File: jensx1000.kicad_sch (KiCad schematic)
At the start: 0 parts

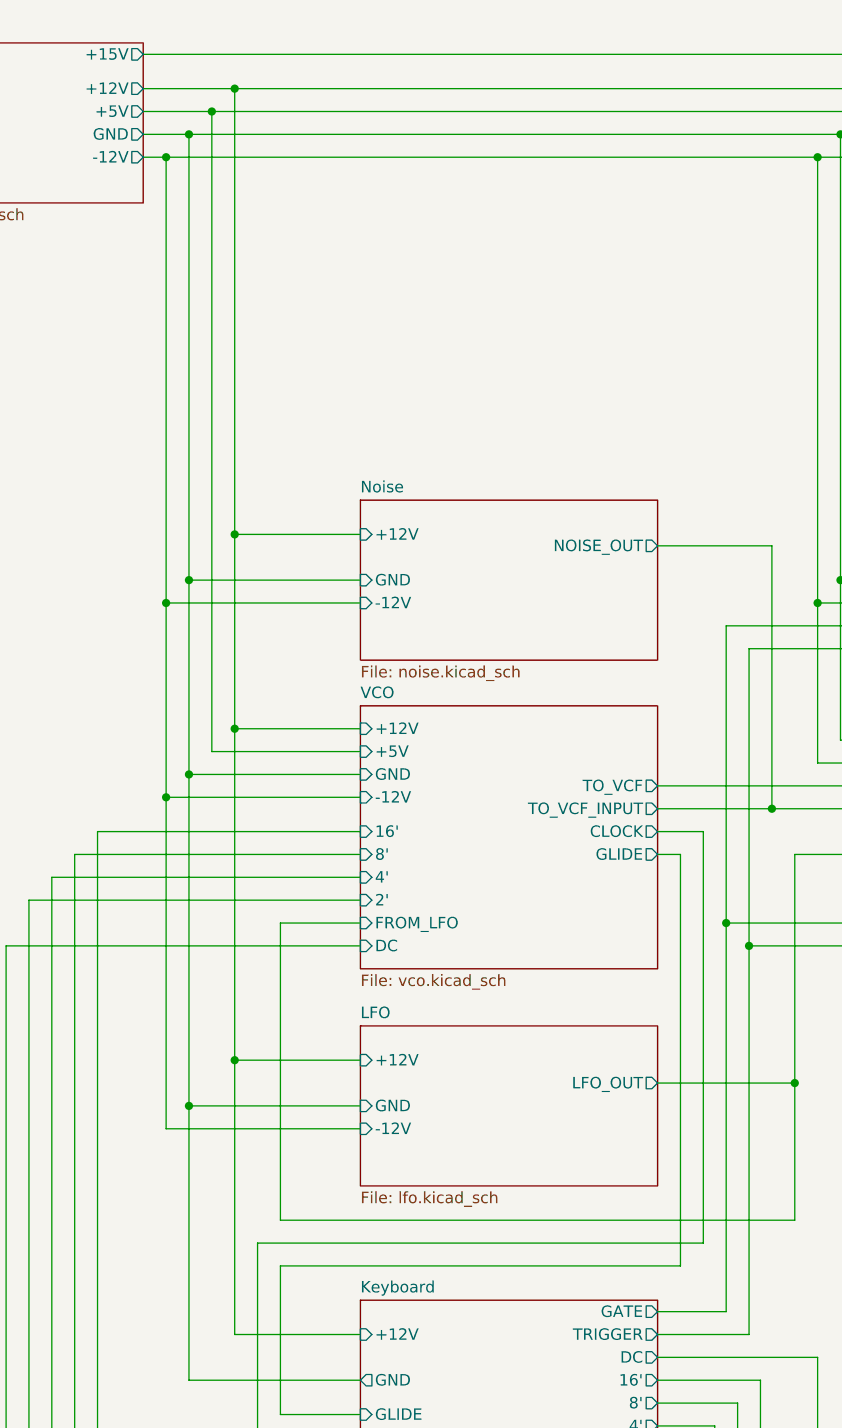
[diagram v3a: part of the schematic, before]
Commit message: Added layout photos, noise & ADSR components are in position
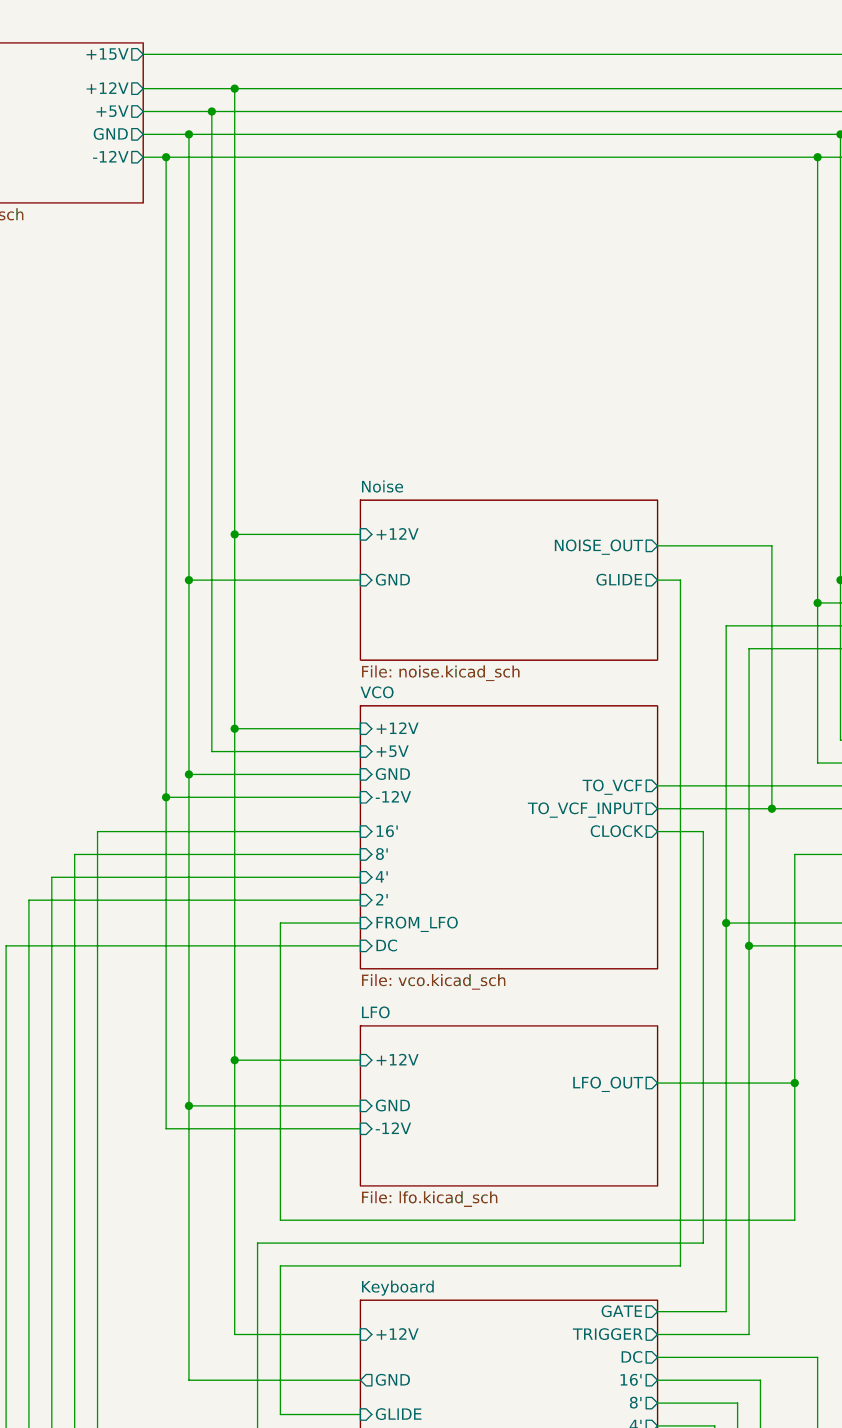
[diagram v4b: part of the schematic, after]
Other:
- sheet Noise ports: added GLIDE; removed -12V
- sheet VCO ports: added none; removed GLIDE
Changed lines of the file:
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@@
-	)
-	(junction
-		(at 49.53 80.01)
-		(diameter 0)
-		(color 0 0 0 0)
 	)
 	(junction
@@
 	(wire
 		(pts
-			(xy 49.53 80.01) (xy 49.53 101.6)
-		)
-		(stroke
-			(width 0)
-			(type default)
-		)
-	)
-	(wire
-		(pts
 			(xy 104.14 105.41) (xy 109.22 105.41)
 		)
@@
 	(wire
 		(pts
+			(xy 106.68 77.47) (xy 106.68 153.67)
+		)
+		(stroke
+			(width 0)
+			(type default)
+		)
+	)
+	(wire
+		(pts
 			(xy 114.3 118.11) (xy 114.3 161.29)
 		)
@@
 	(wire
 		(pts
-			(xy 106.68 153.67) (xy 106.68 107.95)
-		)
-		(stroke
-			(width 0)
-			(type default)
-		)
-	)
-	(wire
-		(pts
 			(xy 172.72 113.03) (xy 129.54 113.03)
 		)
@@
 	(wire
 		(pts
-			(xy 49.53 30.48) (xy 49.53 80.01)
+			(xy 49.53 30.48) (xy 49.53 101.6)
 		)
 		(stroke
@@
 	(wire
 		(pts
-			(xy 49.53 80.01) (xy 71.12 80.01)
-		)
-		(stroke
-			(width 0)
-			(type default)
-		)
-	)
-	(wire
-		(pts
 			(xy 129.54 92.71) (xy 129.54 72.39)
 		)
@@
 	(wire
 		(pts
-			(xy 106.68 107.95) (xy 104.14 107.95)
-		)
-		(stroke
-			(width 0)
-			(type default)
-		)
-	)
-	(wire
-		(pts
 			(xy 104.14 166.37) (xy 115.57 166.37)
 		)
@@
 		(pts
 			(xy 193.04 69.85) (xy 190.5 69.85)
+		)
+		(stroke
+			(width 0)
+			(type default)
+		)
+	)
+	(wire
+		(pts
+			(xy 106.68 77.47) (xy 104.14 77.47)
 		)
 		(stroke
@@
 			)
 		)
-		(pin "GLIDE" output
-			(at 104.14 107.95 0)
-			(effects
-				(font
-					(size 1.27 1.27)
-				)
-				(justify right)
-			)
-		)
 		(instances
 			(project "jensx1000"
@@
 			)
 		)
-		(pin "-12V" input
-			(at 71.12 80.01 180)
-			(effects
-				(font
-					(size 1.27 1.27)
-				)
-				(justify left)
-			)
-		)
 		(pin "GND" input
 			(at 71.12 77.47 180)
@@
 			(effects
 				(font
+					(size 1.27 1.27)
+				)
+				(justify right)
+			)
+		)
+		(pin "GLIDE" output
+			(at 104.14 77.47 0)
+			(effects
+				(font

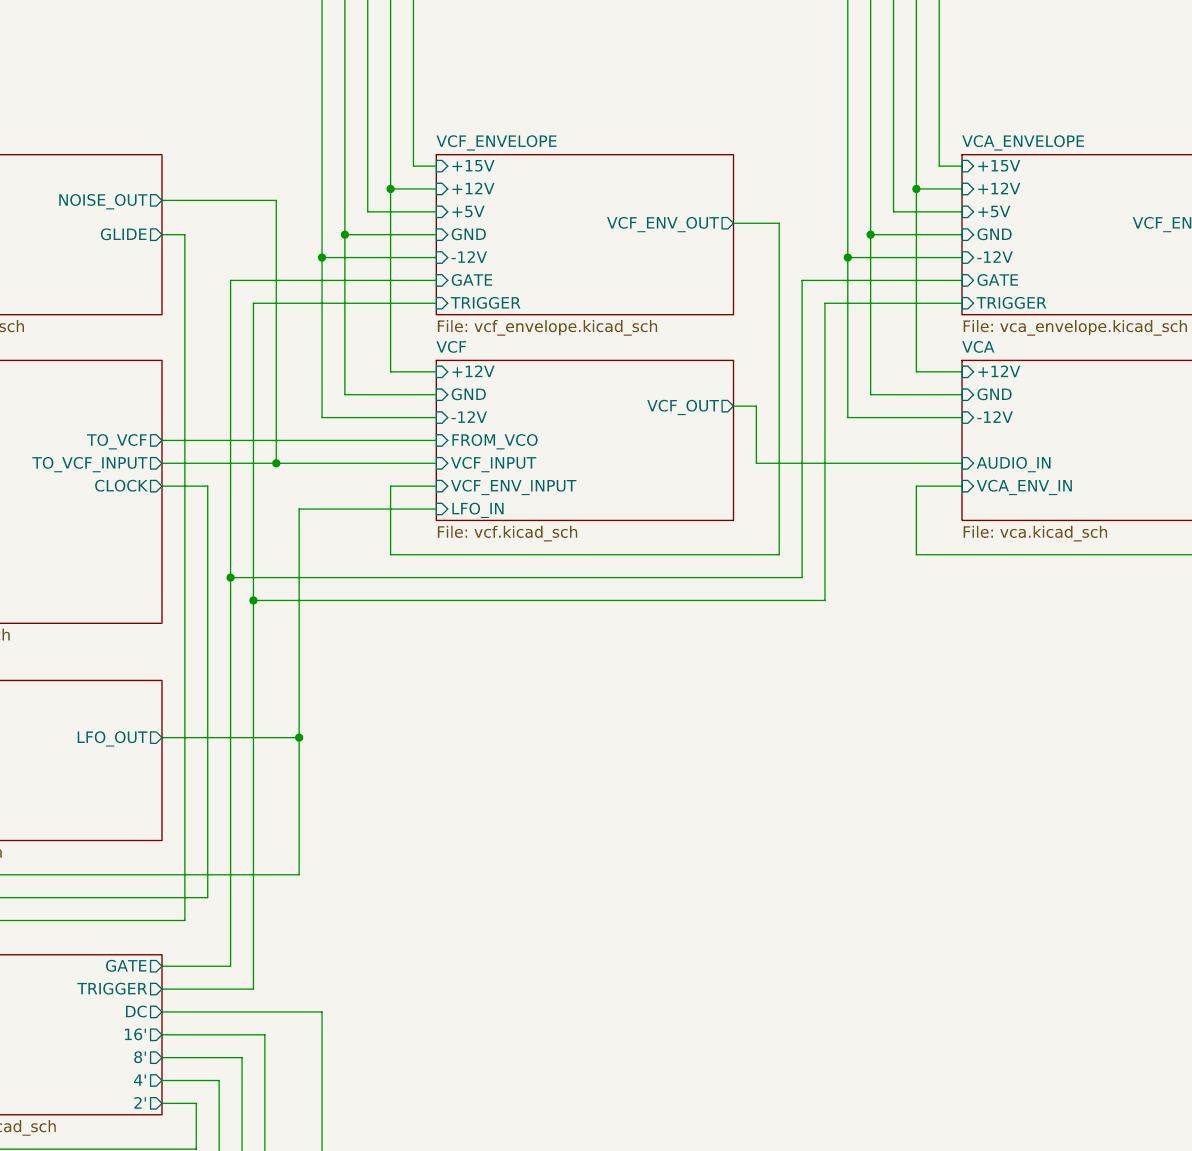
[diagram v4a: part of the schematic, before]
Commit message: Fixed VCF TRIG/GATE net, routed all except keyboard
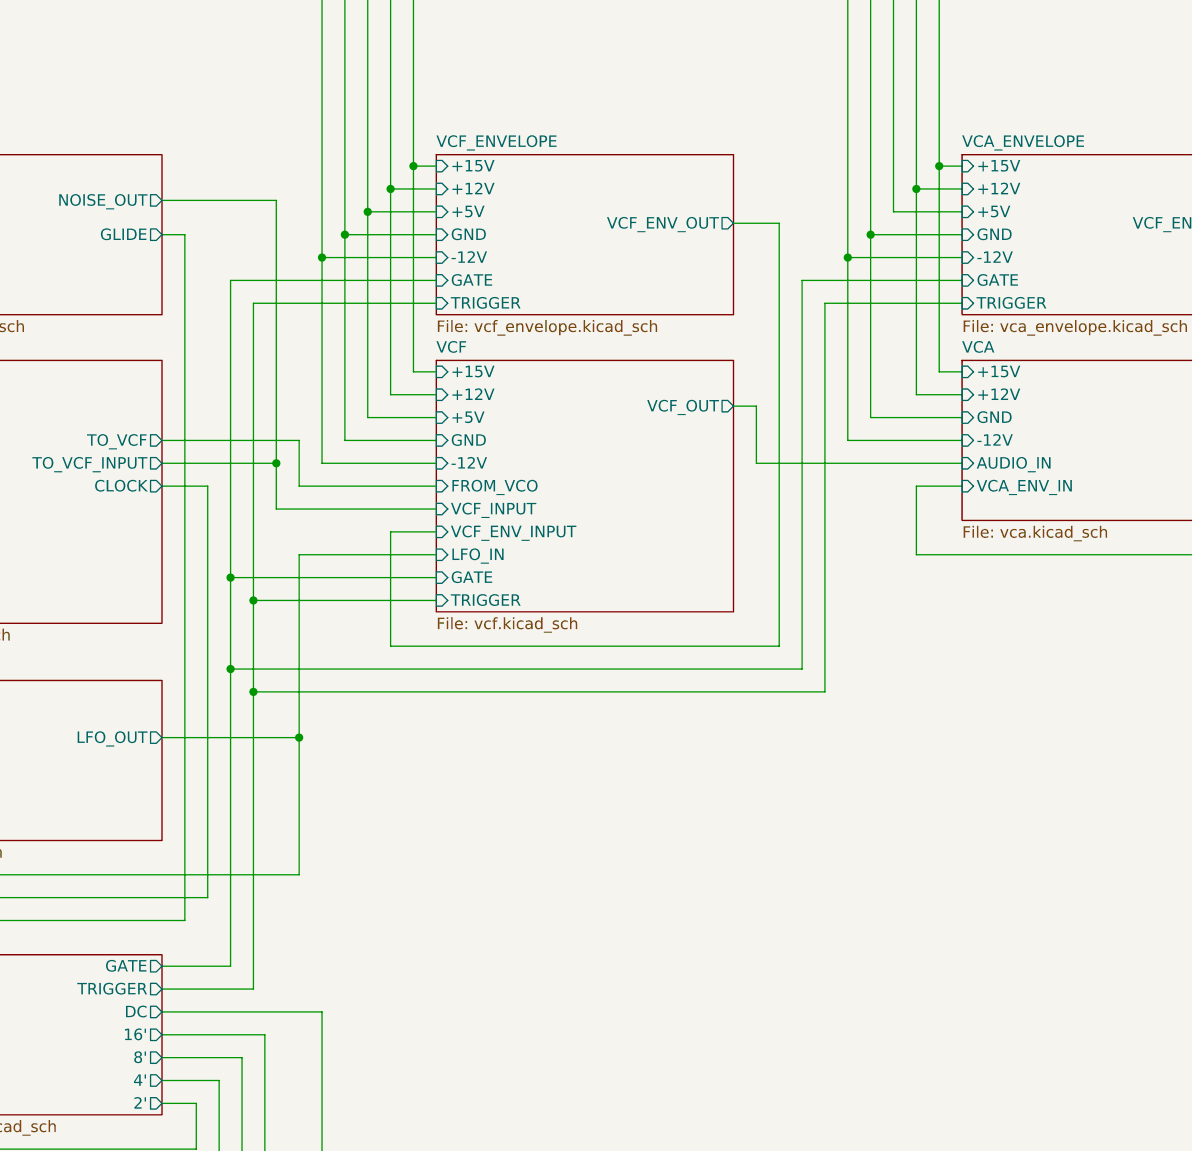
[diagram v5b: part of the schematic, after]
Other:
- sheet VCA ports: added +15V; removed none
- sheet VCF ports: added +15V, +5V, GATE, TRIGGER; removed none

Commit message: Update README, add license to sheets
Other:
- title: (none) -> JEN SX-1000
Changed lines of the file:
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@@
 	(generator_version "9.0")
 	(paper "A4")
+	(title_block
+		(title "JEN SX-1000")
+		(comment 1 "SPDX-License-Identifier: CERN-OHL-S-2.0")
+	)
 	(junction
 		(at 124.46 27.94)

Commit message: Update sheets
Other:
- company: (none) -> Csaba Nagy
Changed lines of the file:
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@@
 	(title_block
 		(title "JEN SX-1000")
+		(company "Csaba Nagy")
 		(comment 1 "SPDX-License-Identifier: CERN-OHL-S-2.0")
 	)
